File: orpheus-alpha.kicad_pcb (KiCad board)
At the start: 2 copper layers, 84.8 x 54.4 mm, 60 parts, among them J1 Signal in, J2 AC in, J3 Signal out, J4 uC, U1 OPA2134, U2 PGA2311, U3 LM317_3PinPackage, U4 LM337_SOT223, U5 LM7805_TO220

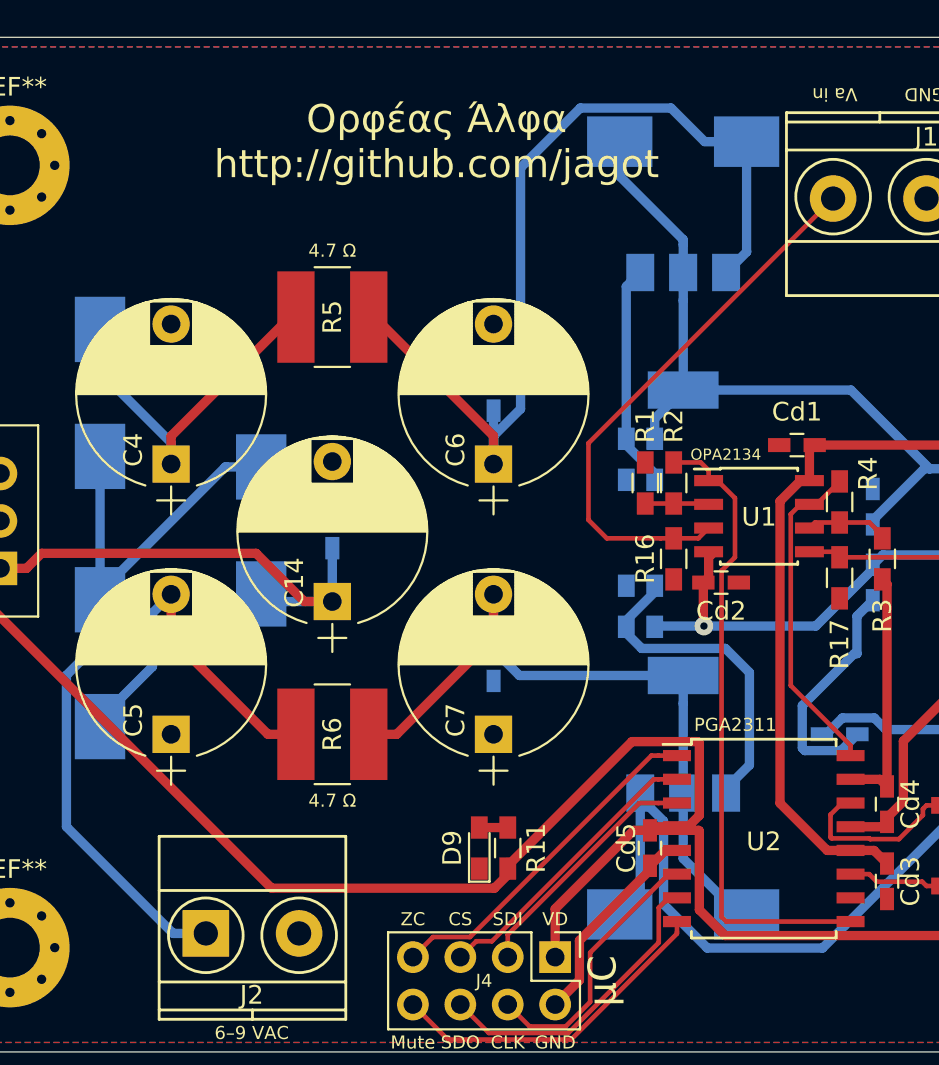
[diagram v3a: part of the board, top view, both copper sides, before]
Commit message: Added optional power connectors
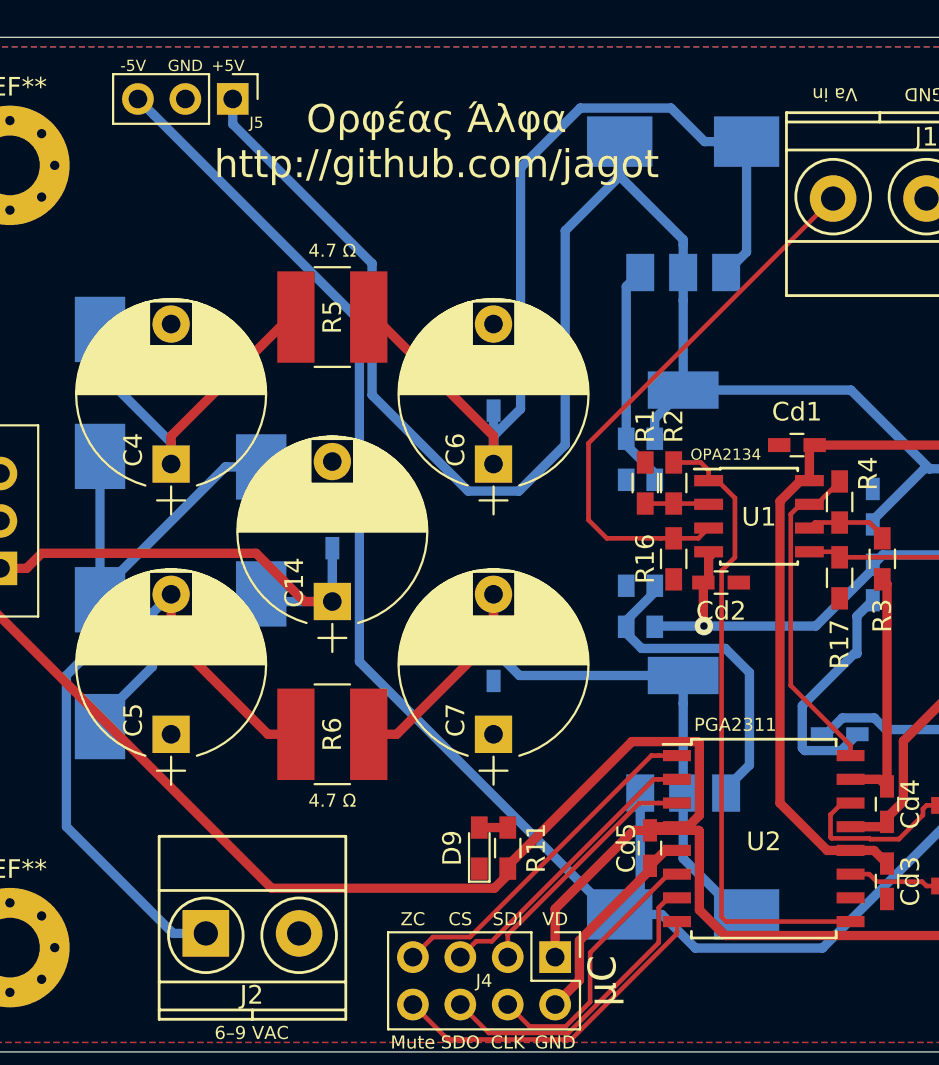
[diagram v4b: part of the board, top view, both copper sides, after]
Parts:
- added J5: CONN_01X03, Pin_Headers:Pin_Header_Straight_1x03_Pitch2.54mm, F.Cu at (103.4, 81.5)
- R10, R7: value 910 -> 330
- R12, R13: value 300 -> 330
- R8, R9: value 2k7 -> 1k
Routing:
- net V-: track 97.8 -> 148.3 mm
- net V+: track 83.7 -> 131.7 mm
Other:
- board text added: "+5V"
- board text added: "-5V"
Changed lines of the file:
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@@
   (general
     (thickness 1.6)
-    (drawings 28)
-    (tracks 297)
+    (drawings 31)
+    (tracks 309)
     (zones 0)
-    (modules 60)
+    (modules 61)
     (nets 32)
   )
@@
       (effects (font (size 1 1) (thickness 0.15)) (justify mirror))
     )
-    (fp_text value 910 (at 0 -1.55 270) (layer B.Fab)
+    (fp_text value 330 (at 0 -1.55 270) (layer B.Fab)
       (effects (font (size 1 1) (thickness 0.15)) (justify mirror))
     )
@@
       (effects (font (size 1 1) (thickness 0.15)) (justify mirror))
     )
-    (fp_text value 2k7 (at 0 -1.55 270) (layer B.Fab)
+    (fp_text value 1k (at 0 -1.55 270) (layer B.Fab)
       (effects (font (size 1 1) (thickness 0.15)) (justify mirror))
     )
@@
       (effects (font (size 1 1) (thickness 0.15)) (justify mirror))
     )
-    (fp_text value 2k7 (at 0 -1.55 270) (layer B.Fab)
+    (fp_text value 1k (at 0 -1.55 270) (layer B.Fab)
       (effects (font (size 1 1) (thickness 0.15)) (justify mirror))
     )
@@
       (effects (font (size 1 1) (thickness 0.15)) (justify mirror))
     )
-    (fp_text value 910 (at -0.254 1.524 270) (layer B.Fab)
+    (fp_text value 330 (at -0.254 1.524 270) (layer B.Fab)
       (effects (font (size 1 1) (thickness 0.15)) (justify mirror))
     )
@@
       (effects (font (size 1 1) (thickness 0.15)))
     )
-    (fp_text value 300 (at 0 1.55) (layer F.Fab)
+    (fp_text value 330 (at 0 1.55) (layer F.Fab)
       (effects (font (size 1 1) (thickness 0.15)))
     )
@@
       (effects (font (size 1 1) (thickness 0.15)))
     )
-    (fp_text value 300 (at 0 1.55) (layer F.Fab)
+    (fp_text value 330 (at 0 1.55) (layer F.Fab)
       (effects (font (size 1 1) (thickness 0.15)))
     )
@@
     )
   )
+  (module Pin_Headers:Pin_Header_Straight_1x03_Pitch2.54mm (layer F.Cu)
+    (at 103.378 81.534 270)
+    (descr "Through hole straight pin header, 1x03, 2.54mm pitch, single row")
+    (tags "Through hole pin header THT 1x03 2.54mm single row")
+    (fp_text reference J5 (at 1.27 -1.27) (layer F.SilkS)
+      (effects (font (size 0.6 0.6) (thickness 0.15)))
+    )
+    (fp_text value CONN_01X03 (at 0 7.41 270) (layer F.Fab)
+      (effects (font (size 1 1) (thickness 0.15)))
+    )
+    (fp_text user %R (at 0 2.54) (layer F.Fab)
+      (effects (font (size 1 1) (thickness 0.15)))
+    )
+    (fp_line (start 1.8 -1.8) (end -1.8 -1.8) (layer F.CrtYd) (width 0.05))
+    (fp_line (start 1.8 6.85) (end 1.8 -1.8) (layer F.CrtYd) (width 0.05))
+    (fp_line (start -1.8 6.85) (end 1.8 6.85) (layer F.CrtYd) (width 0.05))
+    (fp_line (start -1.8 -1.8) (end -1.8 6.85) (layer F.CrtYd) (width 0.05))
+    (fp_line (start -1.33 -1.33) (end 0 -1.33) (layer F.SilkS) (width 0.12))
+    (fp_line (start -1.33 0) (end -1.33 -1.33) (layer F.SilkS) (width 0.12))
+    (fp_line (start -1.33 1.27) (end 1.33 1.27) (layer F.SilkS) (width 0.12))
+    (fp_line (start 1.33 1.27) (end 1.33 6.41) (layer F.SilkS) (width 0.12))
+    (fp_line (start -1.33 1.27) (end -1.33 6.41) (layer F.SilkS) (width 0.12))
+    (fp_line (start -1.33 6.41) (end 1.33 6.41) (layer F.SilkS) (width 0.12))
+    (fp_line (start -1.27 -0.635) (end -0.635 -1.27) (layer F.Fab) (width 0.1))
+    (fp_line (start -1.27 6.35) (end -1.27 -0.635) (layer F.Fab) (width 0.1))
+    (fp_line (start 1.27 6.35) (end -1.27 6.35) (layer F.Fab) (width 0.1))
+    (fp_line (start 1.27 -1.27) (end 1.27 6.35) (layer F.Fab) (width 0.1))
+    (fp_line (start -0.635 -1.27) (end 1.27 -1.27) (layer F.Fab) (width 0.1))
+    (pad 3 thru_hole oval (at 0 5.08 270) (size 1.7 1.7) (drill 1) (layers *.Cu *.Mask)
+      (net 3 V-))
+    (pad 2 thru_hole oval (at 0 2.54 270) (size 1.7 1.7) (drill 1) (layers *.Cu *.Mask)
+      (net 2 GNDA))
+    (pad 1 thru_hole rect (at 0 0 270) (size 1.7 1.7) (drill 1) (layers *.Cu *.Mask)
+      (net 1 V+))
+    (model ${KISYS3DMOD}/Pin_Headers.3dshapes/Pin_Header_Straight_1x03_Pitch2.54mm.wrl
+      (at (xyz 0 0 0))
+      (scale (xyz 1 1 1))
+      (rotate (xyz 0 0 0))
+    )
+  )
+  (gr_text GND (at 100.838 79.756) (layer F.SilkS)
+    (effects (font (size 0.6 0.6) (thickness 0.15)))
+  )
+  (gr_text -5V (at 98.044 79.756) (layer F.SilkS)
+    (effects (font (size 0.6 0.6) (thickness 0.15)))
+  )
+  (gr_text +5V (at 103.124 79.756) (layer F.SilkS)
+    (effects (font (size 0.6 0.6) (thickness 0.15)))
+  )
   (gr_text μC (at 123.19 128.778 90) (layer F.SilkS)
     (effects (font (size 1.5 1.5) (thickness 0.3)))
@@
     (effects (font (size 1.5 1.5) (thickness 0.3)))
   )
+  (segment (start 124.108 83.82) (end 124.108 85.67) (width 0.5) (layer B.Cu) (net 1))
+  (segment (start 115.987999 102.542001) (end 110.841991 97.395993) (width 0.5) (layer B.Cu) (net 1))
+  (segment (start 110.841991 97.395993) (end 110.841991 90.347991) (width 0.5) (layer B.Cu) (net 1))
+  (segment (start 124.108 85.67) (end 121.18796 88.59004) (width 0.5) (layer B.Cu) (net 1))
+  (segment (start 121.18796 88.59004) (end 121.18796 100.062042) (width 0.5) (layer B.Cu) (net 1))
+  (segment (start 121.18796 100.062042) (end 118.708001 102.542001) (width 0.5) (layer B.Cu) (net 1))
+  (segment (start 118.708001 102.542001) (end 115.987999 102.542001) (width 0.5) (layer B.Cu) (net 1))
+  (segment (start 110.841991 90.347991) (end 103.378 82.884) (width 0.5) (layer B.Cu) (net 1))
+  (segment (start 103.378 82.884) (end 103.378 81.534) (width 0.5) (layer B.Cu) (net 1))
   (segment (start 138.43 122.494) (end 137.729 121.793) (width 0.5) (layer F.Cu) (net 1))
   (segment (start 137.729 121.793) (end 136.476 121.793) (width 0.5) (layer F.Cu) (net 1))
@@
   (segment (start 127.508 90.83) (end 127.508 92.33) (width 0.5) (layer B.Cu) (net 1))
   (segment (start 127.508 92.33) (end 127.508 97.13) (width 0.5) (layer B.Cu) (net 1))
-  (segment (start 124.108 83.82) (end 124.108 85.67) (width 0.5) (layer B.Cu) (net 1))
   (segment (start 124.108 85.67) (end 127.508 89.07) (width 0.5) (layer B.Cu) (net 1))
   (segment (start 127.508 89.07) (end 127.508 89.33) (width 0.5) (layer B.Cu) (net 1))
@@
   (segment (start 136.82 111.252) (end 136.82 109.24) (width 0.5) (layer B.Cu) (net 2))
   (segment (start 136.82 109.24) (end 137.668 108.392) (width 0.5) (layer B.Cu) (net 2))
+  (segment (start 124.108 125.222) (end 126.358 125.222) (width 0.5) (layer B.Cu) (net 3))
+  (segment (start 126.358 125.222) (end 128.158001 127.022001) (width 0.5) (layer B.Cu) (net 3))
+  (segment (start 128.158001 127.022001) (end 134.976001 127.022001) (width 0.5) (layer B.Cu) (net 3))
+  (segment (start 134.976001 127.022001) (end 145.522001 116.476001) (width 0.5) (layer B.Cu) (net 3))
+  (segment (start 145.522001 116.476001) (end 145.522001 107.208001) (width 0.5) (layer B.Cu) (net 3))
+  (segment (start 145.522001 107.208001) (end 145.071999 106.757999) (width 0.5) (layer B.Cu) (net 3))
+  (segment (start 145.071999 106.757999) (end 144.272 105.958) (width 0.5) (layer B.Cu) (net 3))
+  (segment (start 124.108 125.222) (end 123.708 125.222) (width 0.5) (layer B.Cu) (net 3))
+  (segment (start 110.162001 111.676001) (end 110.162001 93.398001) (width 0.5) (layer B.Cu) (net 3))
+  (segment (start 123.708 125.222) (end 110.162001 111.676001) (width 0.5) (layer B.Cu) (net 3))
+  (segment (start 110.162001 93.398001) (end 99.147999 82.383999) (width 0.5) (layer B.Cu) (net 3))
+  (segment (start 99.147999 82.383999) (end 98.298 81.534) (width 0.5) (layer B.Cu) (net 3))
   (segment (start 144.272 105.958) (end 145.522001 107.208001) (width 0.5) (layer F.Cu) (net 3))
   (segment (start 145.522001 107.208001) (end 145.522001 109.715997) (width 0.5) (layer F.Cu) (net 3))
@@
   (segment (start 138.171 120.523) (end 138.43 120.264) (width 0.5) (layer F.Cu) (net 3))
   (segment (start 125.208 118.72) (end 125.208 118.97) (width 0.5) (layer B.Cu) (net 3))
-  (segment (start 126.458 124.682002) (end 128.797999 127.022001) (width 0.5) (layer B.Cu) (net 3))
-  (segment (start 125.208 118.97) (end 126.458 120.22) (width 0.5) (layer B.Cu) (net 3))
-  (segment (start 126.458 120.22) (end 126.458 124.682002) (width 0.5) (layer B.Cu) (net 3))
-  (segment (start 128.797999 127.022001) (end 134.976001 127.022001) (width 0.5) (layer B.Cu) (net 3))
-  (segment (start 134.976001 127.022001) (end 145.522001 116.476001) (width 0.5) (layer B.Cu) (net 3))
-  (segment (start 145.522001 116.476001) (end 145.522001 107.208001) (width 0.5) (layer B.Cu) (net 3))
-  (segment (start 145.522001 107.208001) (end 145.071999 106.757999) (width 0.5) (layer B.Cu) (net 3))
-  (segment (start 145.071999 106.757999) (end 144.272 105.958) (width 0.5) (layer B.Cu) (net 3))
   (segment (start 125.208 118.72) (end 125.208 124.122) (width 0.5) (layer B.Cu) (net 3))
   (segment (start 125.208 124.122) (end 124.108 125.222) (width 0.5) (layer B.Cu) (net 3))

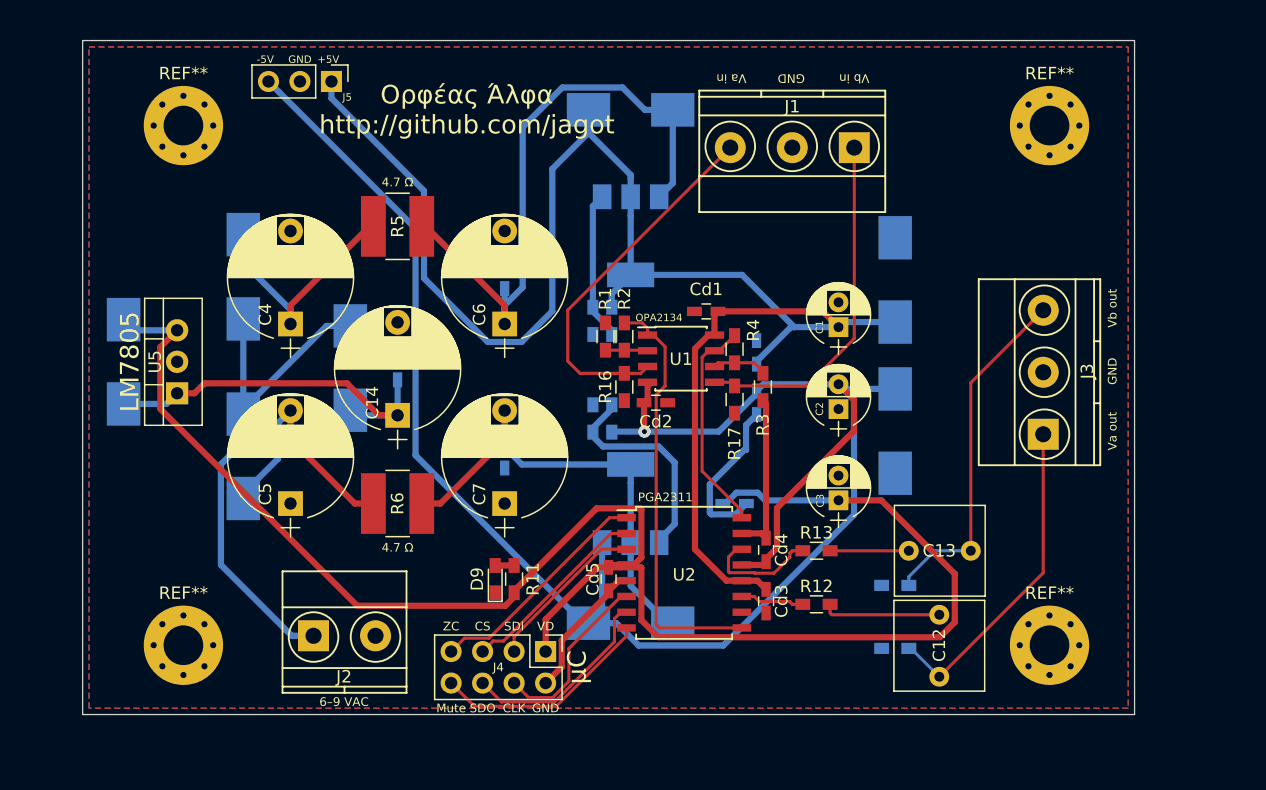
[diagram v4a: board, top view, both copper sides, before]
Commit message: New layout, "debug" connection pads at the edge
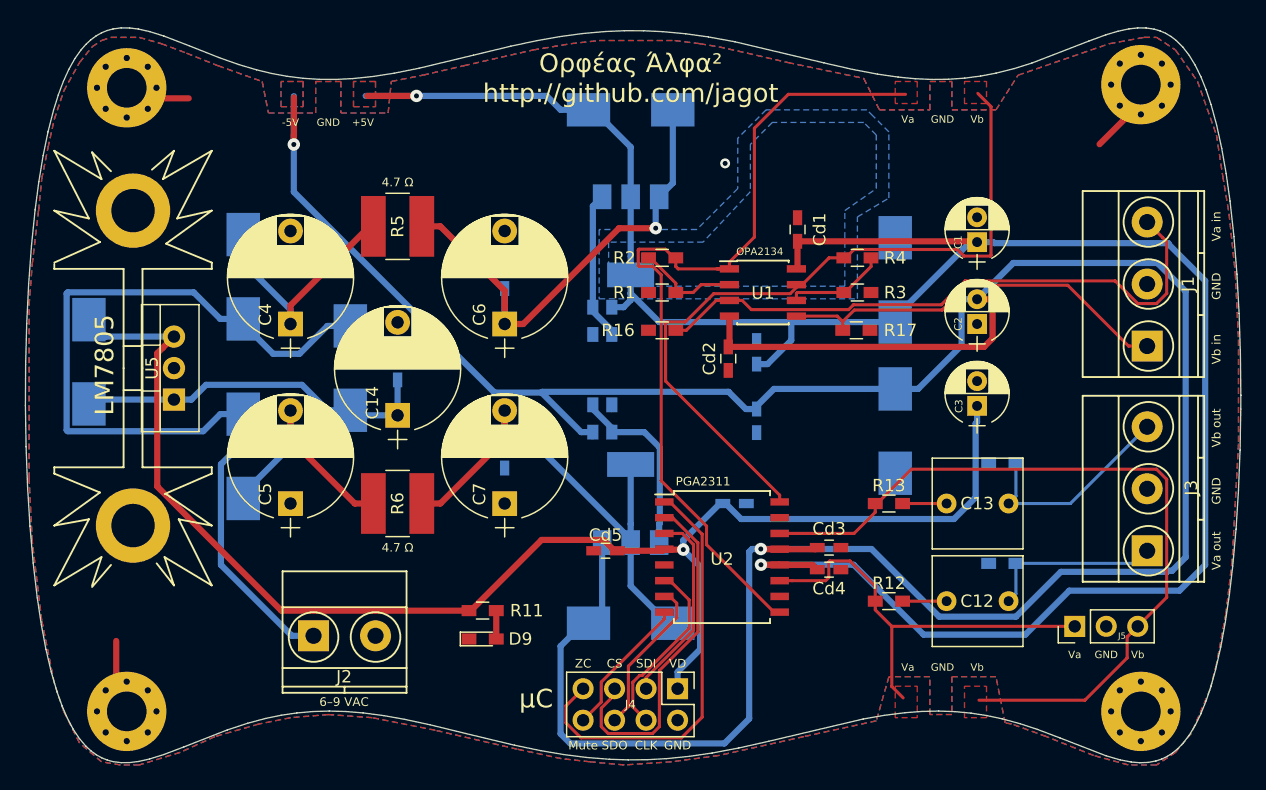
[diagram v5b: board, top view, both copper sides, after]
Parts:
- removed the REF** at (161.3, 127.0)
- removed the REF** at (161.3, 85.1)
- removed the REF** at (91.4, 85.1)
- removed the REF** at (91.4, 127.0)
- added REF**: MountingHole_3.2mm_M3_Pad_Via, Mounting_Holes:MountingHole_3.2mm_M3_Pad_Via, F.Cu at (86.9, 82.0)
- added REF**: MountingHole_3.2mm_M3_Pad_Via, Mounting_Holes:MountingHole_3.2mm_M3_Pad_Via, F.Cu at (86.9, 132.3)
- added REF**: MountingHole_3.2mm_M3_Pad_Via, Mounting_Holes:MountingHole_3.2mm_M3_Pad_Via, F.Cu at (168.7, 81.8)
- added REF**: MountingHole_3.2mm_M3_Pad_Via, Mounting_Holes:MountingHole_3.2mm_M3_Pad_Via, F.Cu at (168.7, 132.3)
- added REF**: Heatsink_Fischer_SK104-STCB_35x13mm__2xDrill3.5mm_ScrewM3, Heatsinks:Heatsink_Fischer_SK104-STCB_35x13mm__2xDrill3.5mm_ScrewM3, F.Cu at (87.4, 104.6)
- moved J5 74.3 mm to (163.3, 125.5), turned to 90 degrees
- moved J1 28.5 mm to (169.2, 102.9), turned to 90 degrees
- moved C3 13.5 mm to (155.4, 107.7)
- moved R15 13.1 mm to (157.5, 112.3)
- moved C1 13.1 mm to (155.4, 94.5)
- moved C2 13.1 mm to (155.4, 101.1)
- moved J3 12.6 mm to (169.2, 119.4)
- moved R4 12.3 mm to (145.8, 95.8), turned to 180 degrees
- moved R17 11.3 mm to (145.7, 101.6), turned to 0 degrees
- moved J4 11.1 mm to (131.3, 130.5)
- moved R14 11.0 mm to (157.5, 120.4)
- moved R3 10.8 mm to (145.8, 98.6), turned to 180 degrees
- moved Cd1 9.89 mm to (141.0, 93.5), turned to 90 degrees
- moved U1 8.49 mm to (138.2, 98.6)
- moved C12 8.27 mm to (158.0, 123.4), turned to 180 degrees
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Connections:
- J5 pad 1: V+ -> Va_amp
- J5 pad 3: V- -> Vb_amp
- R12 pad 1: Net-(R12-Pad1) -> Va_amp
- R13 pad 1: Net-(R13-Pad1) -> Vb_amp
- U2 pad 11: Net-(R12-Pad1) -> Va_amp
- U2 pad 14: Net-(R13-Pad1) -> Vb_amp
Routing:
- net V-: track 148.3 -> 245.9 mm, vias 1 -> 2
- net Vb_amp: track 0.00 -> 63.2 mm
- net V+: track 131.7 -> 183.0 mm, vias 0 -> 2
- net Vb_buf: track 17.6 -> 60.8 mm
- net Va_buf: track 34.6 -> 69.9 mm
- net Va_amp: track 0.00 -> 34.6 mm
- net Vac1: track 42.2 -> 74.8 mm
- net VD: track 136.7 -> 116.2 mm, vias 0 -> 1
- net Va_in: track 29.7 -> 49.4 mm
- net GNDA: track 37.6 -> 20.8 mm, vias 0 -> 1
- net Zcen: track 18.6 -> 34.4 mm
- net CS: track 15.6 -> 28.3 mm
- net Va_out: track 26.4 -> 14.3 mm
- net Net-(C6-Pad1): track 51.8 -> 39.9 mm, vias 0 -> 1
- net Vb_out: track 28.4 -> 17.3 mm
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- added copper zone on B.Cu, net V+
- added copper zone on F.Cu, net V+
- added copper zone on B.Cu, net V-
- added copper zone on F.Cu, net V-
- added copper zone on F.Cu, net Va_amp
- added copper zone on F.Cu, net Va_buf
- added copper zone on F.Cu, net Vb_amp
- added copper zone on F.Cu, net Vb_buf
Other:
- board size 84.8 x 54.4 mm -> 98 x 59.3 mm
- net class signal added: clearance 0.1, trace_width 0.25, via_dia 0.8, via_drill 0.4
- board text added: "Va"
- board text added: "Vb"
- board text added: "Ορφέας Άλφα² http://github.com/jagot"
- board text removed: "Ορφέας Άλφα http://github.com/jagot"

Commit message: Added heatsinks
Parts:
- removed the REF** at (87.4, 104.6)
- U5: footprint TO_SOT_Packages_THT:TO-220_Vertical -> orpheus-alpha:TO-220_Vertical
- moved U3 6.48 mm to (126.2, 87.6), turned to 180 degrees
- moved D3 2.96 mm to (126.0, 81.3)
- moved U4 2.62 mm to (126.2, 117.9), turned to 180 degrees
- moved D4 1.83 mm to (126.0, 124.2), turned to 180 degrees
- moved R10 1.52 mm to (126.0, 108.7)
- moved R9 1.52 mm to (124.5, 108.7)
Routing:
- net Net-(C7-Pad2): track 41.9 -> 14.3 mm
- net V+: track 183.0 -> 157.3 mm
- net Net-(C6-Pad1): track 39.9 -> 53.7 mm, vias 1 -> 0
- net VD: track 116.2 -> 107.1 mm
- net Net-(R7-Pad2): track 12.0 -> 20.4 mm
- net Net-(R10-Pad1): track 15.1 -> 12.0 mm
- net V-: track 245.9 -> 247.9 mm
- added copper zone on B.Cu, net Net-(C7-Pad2)
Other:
- net class Default: clearance 0.1 -> 0
- rule trace_clearance: 0.1 -> 0
